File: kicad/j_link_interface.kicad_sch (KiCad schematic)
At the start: 7 parts, among them J1 Conn_01x05_Pin, J2 SSW-110-02-G-D-RA-N, J3 FTSH-107-01-X-DV-K

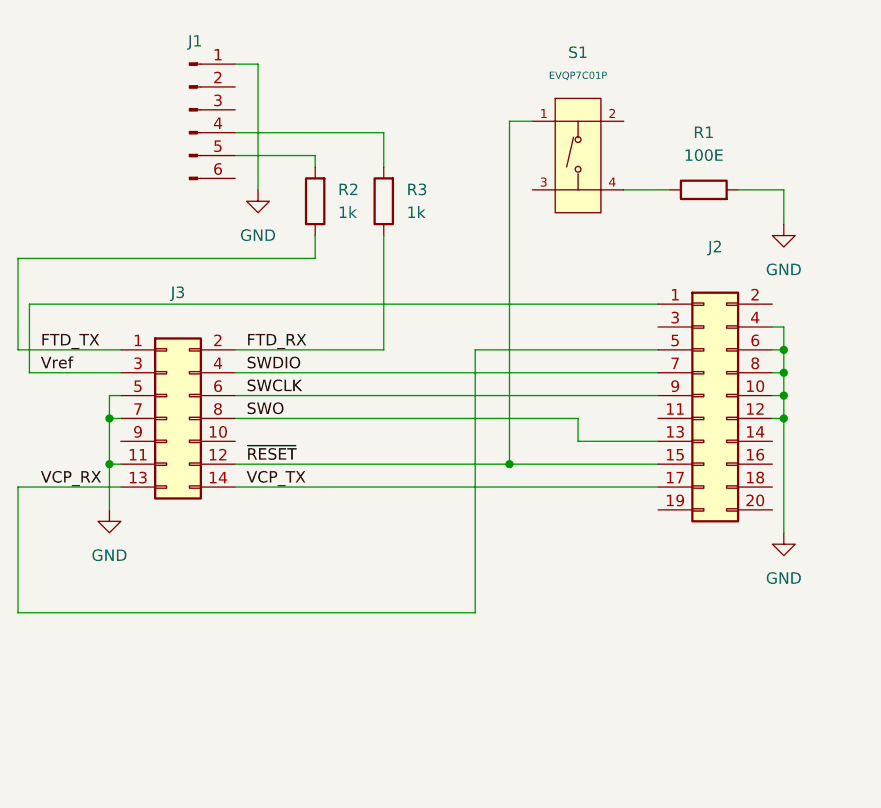
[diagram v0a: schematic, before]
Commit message: Added 2 holes for an enclosure. Moved the reset button.
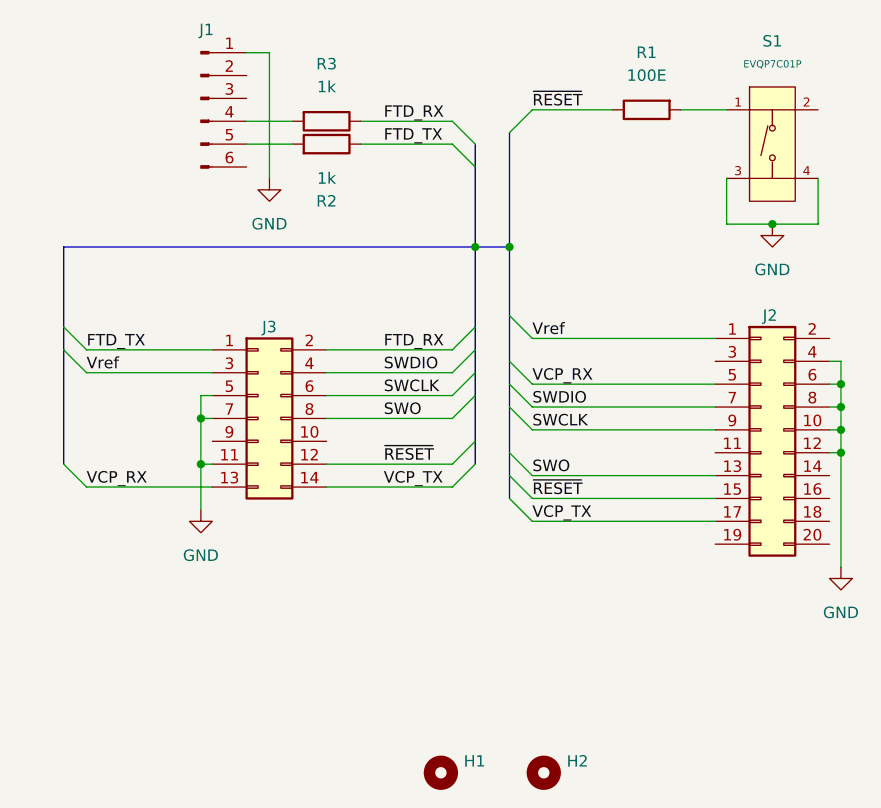
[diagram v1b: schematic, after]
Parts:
- added H1, H2: MountingHole, local_library:MountingHole_2.2mm_M2, symbol Mechanical:MountingHole
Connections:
- net GND: now also S1.3 (C), S1.4 (D); no longer R1.2
- net ~{RESET}: now also R1.1; no longer S1.1 (A)
- new net: R1.2, S1.1 (A)
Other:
- moved on the sheet: J1, J2, J3, R1, R2, R3, S1

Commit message: Swapped Tx/Rx labels for clarity as they were related to the UARTs on the target board. Some minor updates to traces.
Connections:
- net FTD_RX: now also J3.1 (Pin_1), R2.1; no longer J3.2 (Pin_2), R3.1
- net FTD_TX: now also J3.2 (Pin_2), R3.1; no longer J3.1 (Pin_1), R2.1
- net VCP_RX: now also J2.17 (Pin_17), J3.14 (Pin_14); no longer J2.5 (Pin_5), J3.13 (Pin_13)
- net VCP_TX: now also J2.5 (Pin_5), J3.13 (Pin_13); no longer J2.17 (Pin_17), J3.14 (Pin_14)
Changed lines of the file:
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@@
 		)
 	)
-	(label "VCP_TX"
+	(label "VCP_RX"
 		(at 146.05 130.81 0)
 		(effects
@@
 		)
 	)
-	(label "FTD_RX"
+	(label "FTD_TX"
 		(at 129.54 86.36 0)
 		(effects
@@
 		)
 	)
-	(label "FTD_TX"
+	(label "FTD_RX"
 		(at 96.52 111.76 0)
 		(effects
@@
 		)
 	)
-	(label "VCP_RX"
+	(label "VCP_TX"
 		(at 146.05 115.57 0)
 		(effects
@@
 		)
 	)
-	(label "FTD_TX"
+	(label "FTD_RX"
 		(at 129.54 88.9 0)
 		(effects
@@
 		)
 	)
-	(label "VCP_RX"
+	(label "VCP_TX"
 		(at 96.52 127 0)
 		(effects
@@
 		)
 	)
-	(label "VCP_TX"
+	(label "VCP_RX"
 		(at 129.54 127 0)
 		(effects
@@
 		)
 	)
-	(label "FTD_RX"
+	(label "FTD_TX"
 		(at 129.54 111.76 0)
 		(effects
